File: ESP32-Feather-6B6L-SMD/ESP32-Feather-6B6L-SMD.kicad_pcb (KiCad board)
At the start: 2 copper layers, 61 x 78.7 mm, 37 parts, among them J201 RJ45, J202 RJ45, J401 G 6 5 4 3 2 1, J501 + 1 2 3 4 5 6 7 8 -, U201 TCAN332DR, U301 AP63205, U403 74HCT14, U501 TBD62084A

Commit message: Minor tweaks.
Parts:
- moved J401 1.60 mm to (132.4, 95.6)
- moved R412 1.60 mm to (146.3, 95.6)
- moved U403 1.60 mm to (147.6, 104.2)
- moved C401 1.60 mm to (141.5, 104.5)
- moved C402 1.60 mm to (148.8, 109.6)
- moved C403 1.60 mm to (150.1, 98.6)
- moved C404 1.60 mm to (145.0, 98.6)
- moved C405 1.60 mm to (147.6, 98.6)
- moved C406 1.60 mm to (146.3, 109.6)
- moved C407 1.60 mm to (143.8, 109.6)
- moved R401 1.60 mm to (145.0, 112.7)
- moved R402 1.60 mm to (147.6, 112.7)
- moved R409 1.60 mm to (150.1, 112.7)
- moved R410 1.60 mm to (148.8, 95.5)
- moved R411 1.60 mm to (143.8, 95.5)
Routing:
- net GND: track 61.4 -> 50.9 mm
- net /N$14: track 21.7 -> 23.3 mm
- net /N$8: track 24.8 -> 26.4 mm
- net /N$12: track 43.6 -> 45.2 mm
- net /N$9: track 26.0 -> 27.6 mm
- net /N$15: track 26.5 -> 28.1 mm
- net /N$13: track 42.5 -> 44.0 mm
- net Net-(C406-Pad1): track 32.9 -> 32.2 mm
- net /CAN Transceiver/+12V CAN Power: track 108.5 -> 107.9 mm

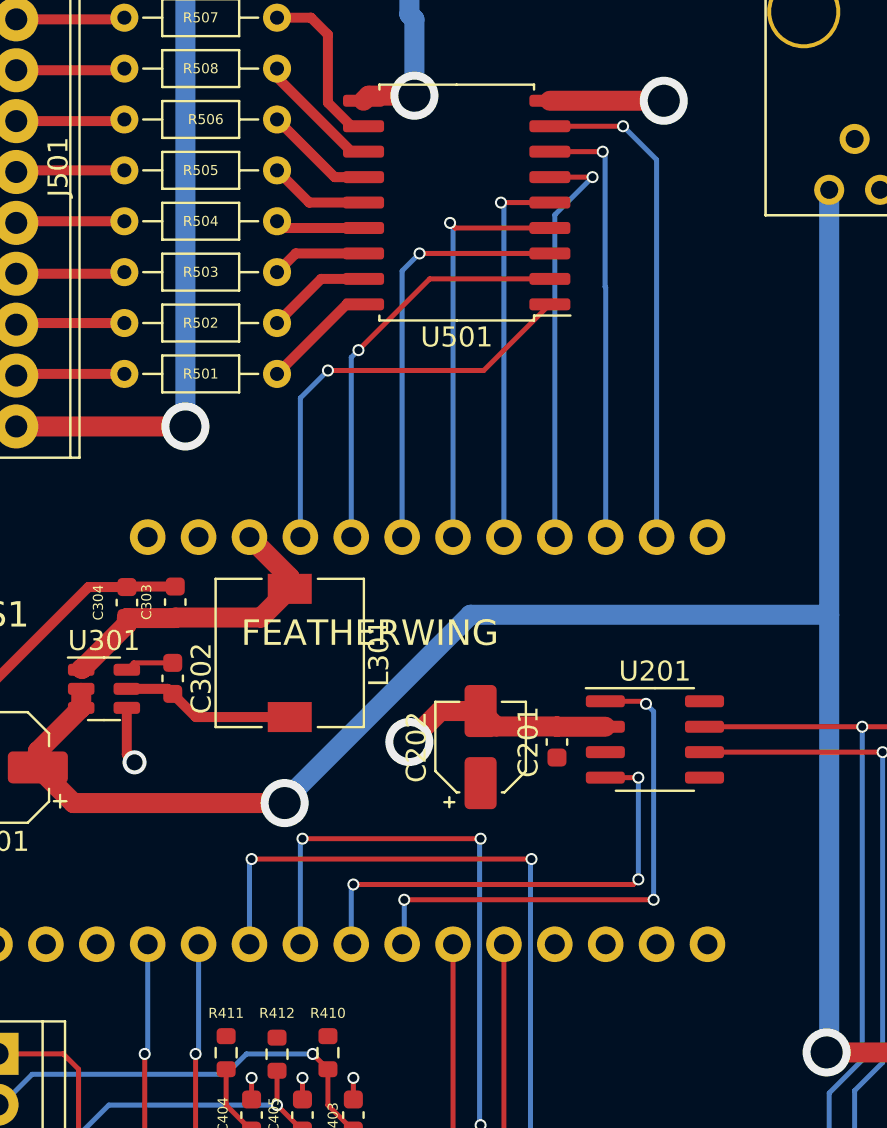
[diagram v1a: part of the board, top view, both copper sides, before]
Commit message: Rescue SCL.
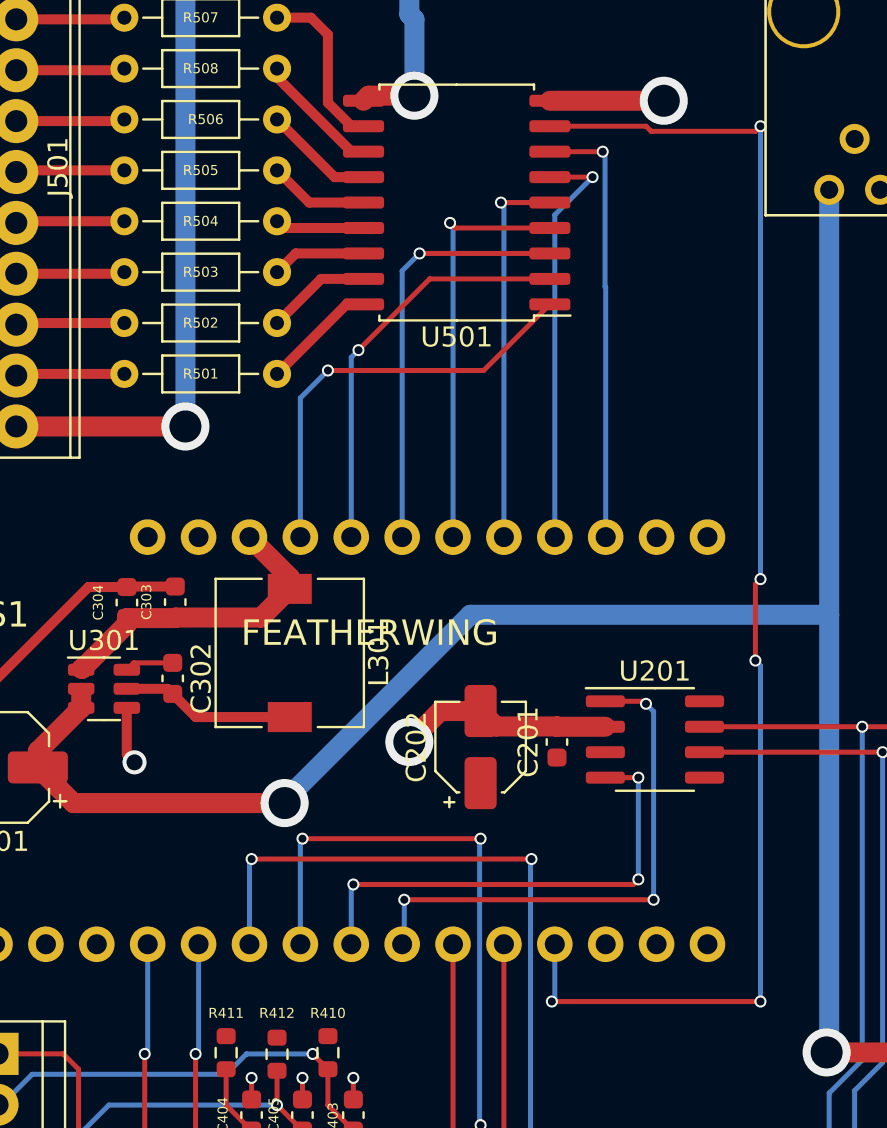
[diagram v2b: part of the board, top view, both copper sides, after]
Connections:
- U501 pad 8: /N$24 -> /N$7
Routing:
- net /N$7: track 0.00 -> 68.0 mm, vias 0 -> 5
- net /N$24: track 24.9 -> 0.00 mm, vias 1 -> 0
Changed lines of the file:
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@@
       (net 3 "/N$23") (pinfunction "In") (pintype "input"))
     (pad "8" smd roundrect (at -4.65 3.81 180) (size 2.05 0.6) (layers "F.Cu" "F.Paste" "F.Mask") (roundrect_rratio 0.25)
-      (net 2 "/N$24") (pinfunction "In") (pintype "input"))
+      (net 20 "/N$7") (pinfunction "In") (pintype "input"))
     (pad "9" smd roundrect (at -4.65 5.08 180) (size 2.05 0.6) (layers "F.Cu" "F.Paste" "F.Mask") (roundrect_rratio 0.25)
       (net 24 "GND") (pinfunction "IC") (pintype "unspecified"))
@@
   )
   (gr_rect (start 187.96 116.84) (end 127 38.1) (layer "Edge.Cuts") (width 0.15) (fill none))
-  (segment (start 159.922 49.276) (end 163.576 49.276) (width 0.25) (layer "F.Cu") (net 2))
-  (via (at 163.576 49.276) (size 0.6) (drill 0.4) (layers "F.Cu" "B.Cu") (net 2))
-  (segment (start 163.576 49.276) (end 165.2484 50.9484) (width 0.25) (layer "B.Cu") (net 2))
-  (segment (start 165.2484 50.9484) (end 165.2484 69.7848) (width 0.25) (layer "B.Cu") (net 2))
   (segment (start 159.922 50.546) (end 162.56 50.546) (width 0.25) (layer "F.Cu") (net 3))
   (via (at 162.56 50.546) (size 0.6) (drill 0.4) (layers "F.Cu" "B.Cu") (net 3))
@@
   (segment (start 157.734 104.724) (end 148.082 104.724) (width 0.25) (layer "B.Cu") (net 19))
   (segment (start 148.082 104.724) (end 147.828 104.978) (width 0.25) (layer "B.Cu") (net 19))
+  (segment (start 164.976324 49.531) (end 170.179 49.531) (width 0.25) (layer "F.Cu") (net 20))
+  (segment (start 159.922 49.276) (end 164.721324 49.276) (width 0.25) (layer "F.Cu") (net 20))
+  (segment (start 164.721324 49.276) (end 164.976324 49.531) (width 0.25) (layer "F.Cu") (net 20))
+  (segment (start 170.18 72.136) (end 170.434 71.882) (width 0.25) (layer "F.Cu") (net 20))
+  (segment (start 170.18 75.946) (end 170.18 72.136) (width 0.25) (layer "F.Cu") (net 20))
+  (segment (start 160.02 92.964) (end 170.434 92.964) (width 0.25) (layer "F.Cu") (net 20))
+  (segment (start 170.179 49.531) (end 170.434 49.276) (width 0.25) (layer "F.Cu") (net 20))
+  (via (at 170.434 92.964) (size 0.6) (drill 0.4) (layers "F.Cu" "B.Cu") (net 20))
+  (via (at 170.18 75.946) (size 0.6) (drill 0.4) (layers "F.Cu" "B.Cu") (net 20))
+  (via (at 160.02 92.964) (size 0.6) (drill 0.4) (layers "F.Cu" "B.Cu") (net 20))
+  (via (at 170.434 49.276) (size 0.6) (drill 0.4) (layers "F.Cu" "B.Cu") (net 20))
+  (via (at 170.434 71.882) (size 0.6) (drill 0.4) (layers "F.Cu" "B.Cu") (net 20))
+  (segment (start 170.434 71.882) (end 170.434 49.276) (width 0.25) (layer "B.Cu") (net 20))
+  (segment (start 170.434 92.964) (end 170.434 76.2) (width 0.25) (layer "B.Cu") (net 20))
+  (segment (start 170.434 76.2) (end 170.18 75.946) (width 0.25) (layer "B.Cu") (net 20))
+  (segment (start 160.1684 90.1048) (end 160.1684 92.8156) (width 0.25) (layer "B.Cu") (net 20))
+  (segment (start 160.1684 92.8156) (end 160.02 92.964) (width 0.25) (layer "B.Cu") (net 20))
   (segment (start 129.966 81.28) (end 129.966 83.865) (width 0.5) (layer "F.Cu") (net 24))
   (segment (start 143.764 110.351) (end 143.764 111.252) (width 0.25) (layer "F.Cu") (net 24))
@@
   (segment (start 133.37 51.4788) (end 133.288 51.5608) (width 0.5) (layer "F.Cu") (net 56))
   (segment (start 138.684 54.0188) (end 133.37 54.0188) (width 0.5) (layer "F.Cu") (net 57))
-  (segment (start 138.602 54.1008) (end 138.684 54.0188) (width 0.25) (layer "F.Cu") (net 57))
   (segment (start 133.37 59.0988) (end 133.288 59.1808) (width 0.5) (layer "F.Cu") (net 58))
   (segment (start 138.684 59.0988) (end 133.37 59.0988) (width 0.5) (layer "F.Cu") (net 58))
